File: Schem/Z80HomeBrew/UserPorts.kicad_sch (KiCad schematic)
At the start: 8 parts, among them J7 Z80HomeBrewUser, J9 Conn_02x10_Odd_Even, U31 MAX202IDR

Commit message: Finally found a name "Zephyr-80" for the brew and committing the first pbc
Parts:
- J7: footprint Connector_PCBEdge:BUS_PCI_Express_Mini -> Connector_PCBEdge:BUS_PCI_Express_Mini_Full
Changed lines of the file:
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@@
 			)
 		)
-		(property "Footprint" "Connector_PCBEdge:BUS_PCI_Express_Mini"
+		(property "Footprint" "Connector_PCBEdge:BUS_PCI_Express_Mini_Full"
 			(at 102.108 199.39 0)
 			(effects
@@
 			)
 		)
-		(property "Footprint" "Connector_PCBEdge:BUS_PCI_Express_Mini"
+		(property "Footprint" "Connector_PCBEdge:BUS_PCI_Express_Mini_Full"
 			(at 230.378 29.21 0)
 			(effects

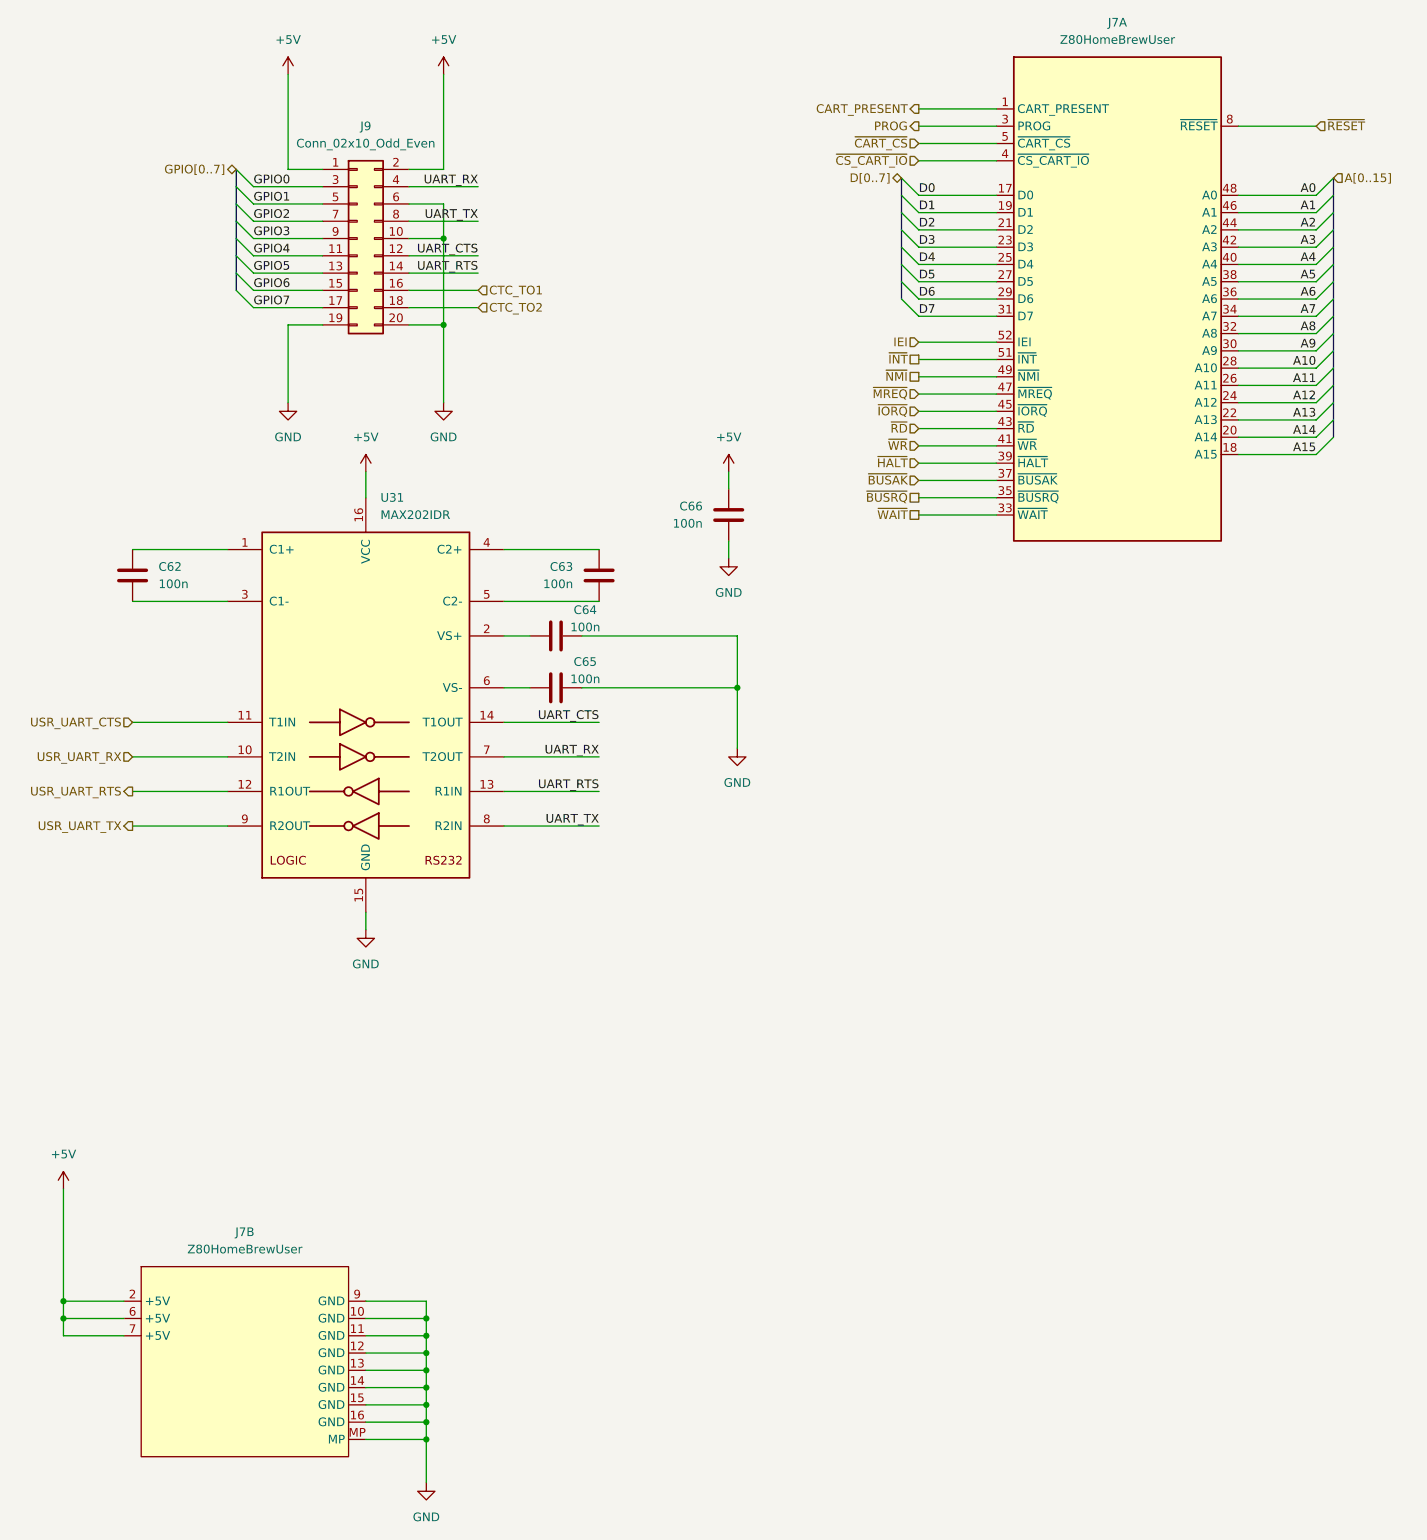
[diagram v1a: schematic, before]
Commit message: Added pBITzBackplane and MezzanineConnector
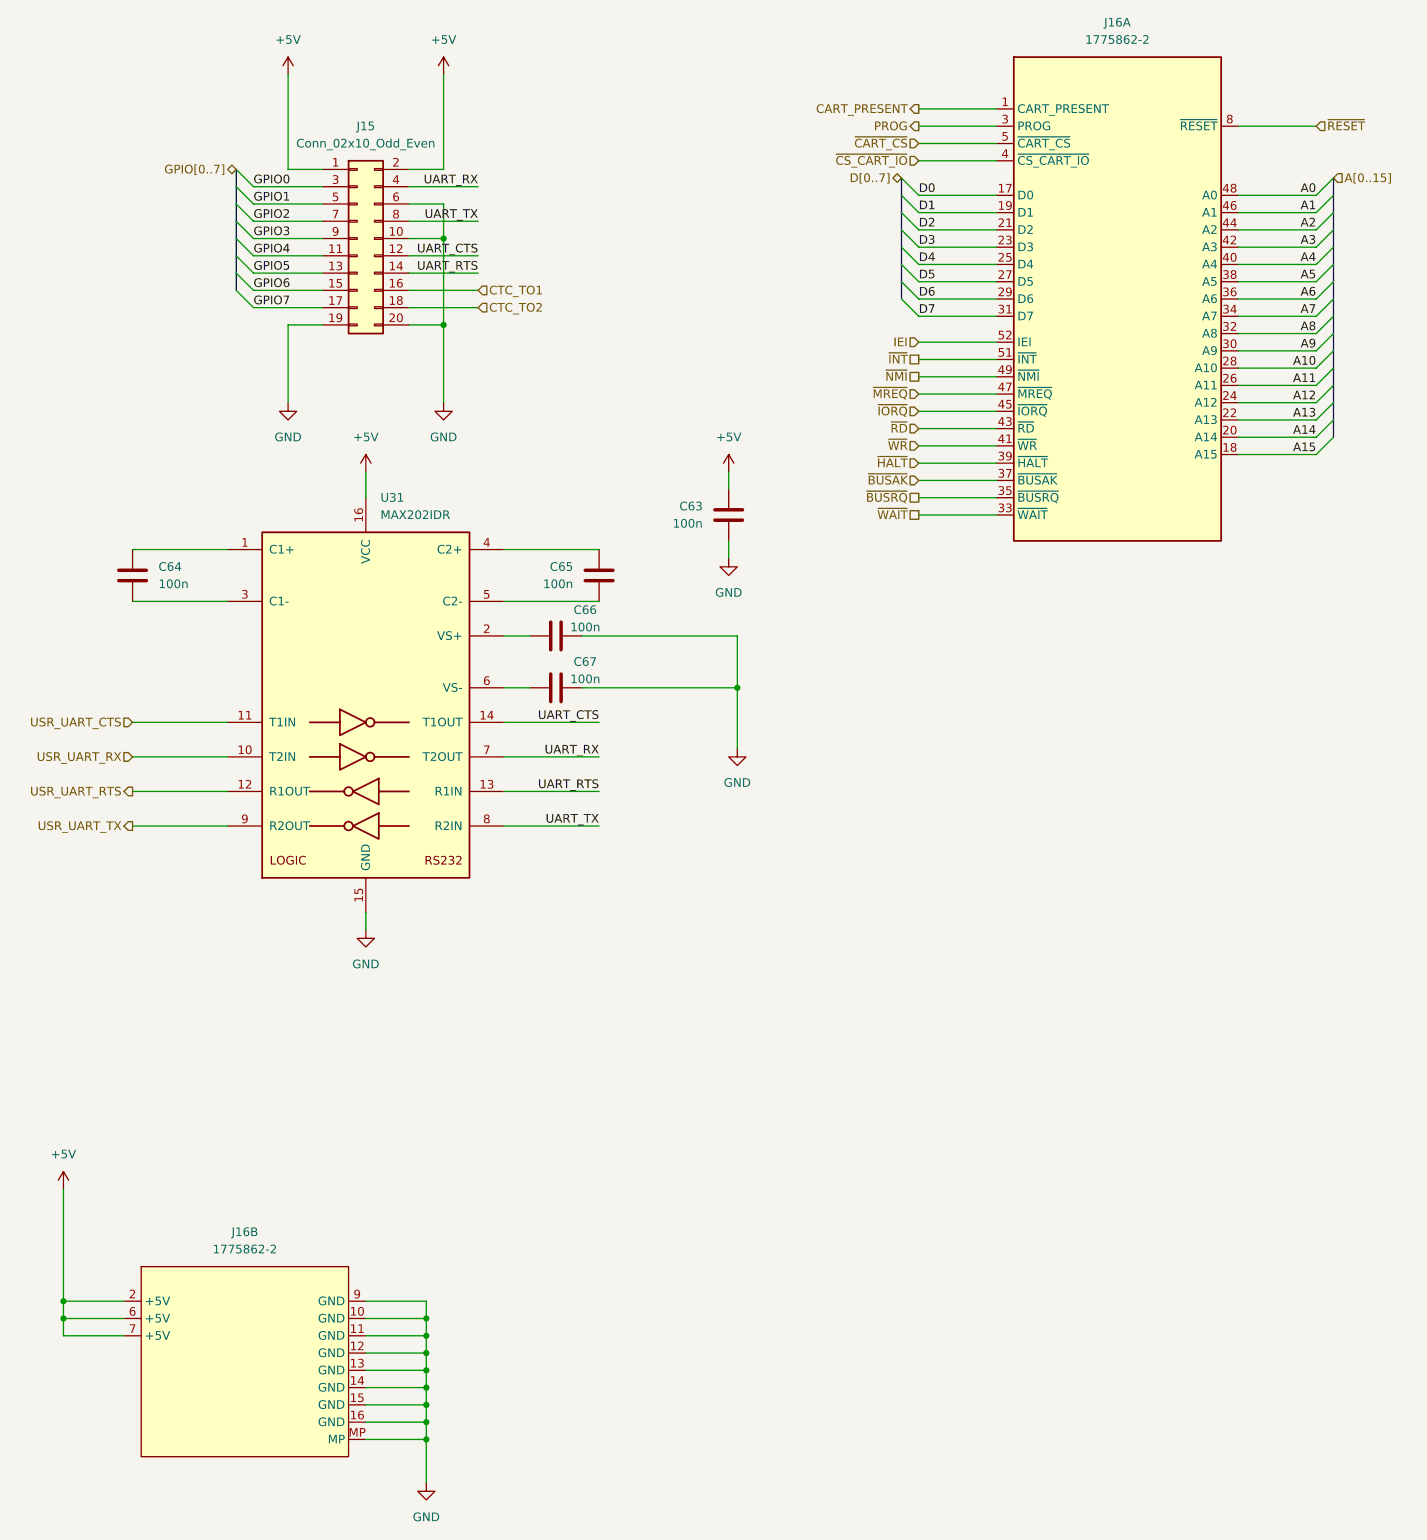
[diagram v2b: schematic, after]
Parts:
- C63: renamed from C66; MANUFACTURER_PART_NUMBER (none) -> C0603C104K5RACTU
- C64: renamed from C62; MANUFACTURER_PART_NUMBER (none) -> C0603C104K5RACTU
- C65: renamed from C63; MANUFACTURER_PART_NUMBER (none) -> C0603C104K5RACTU
- C66: renamed from C64; MANUFACTURER_PART_NUMBER (none) -> C0603C104K5RACTU
- C67: renamed from C65; MANUFACTURER_PART_NUMBER (none) -> C0603C104K5RACTU
- J15: renamed from J9; MANUFACTURER_PART_NUMBER (none) -> ED10524-ND
- J16: renamed from J7; value Z80HomeBrewUser -> 1775862-2; MANUFACTURER_PART_NUMBER (none) -> 1775862-2
- U31: MANUFACTURER_PART_NUMBER (none) -> MAX202IDR
